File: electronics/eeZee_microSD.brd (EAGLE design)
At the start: 18.3 x 19.8 mm, 12 parts, among them U1 MCP1824S, U2 74HC4050, U4 MICROSD_CD

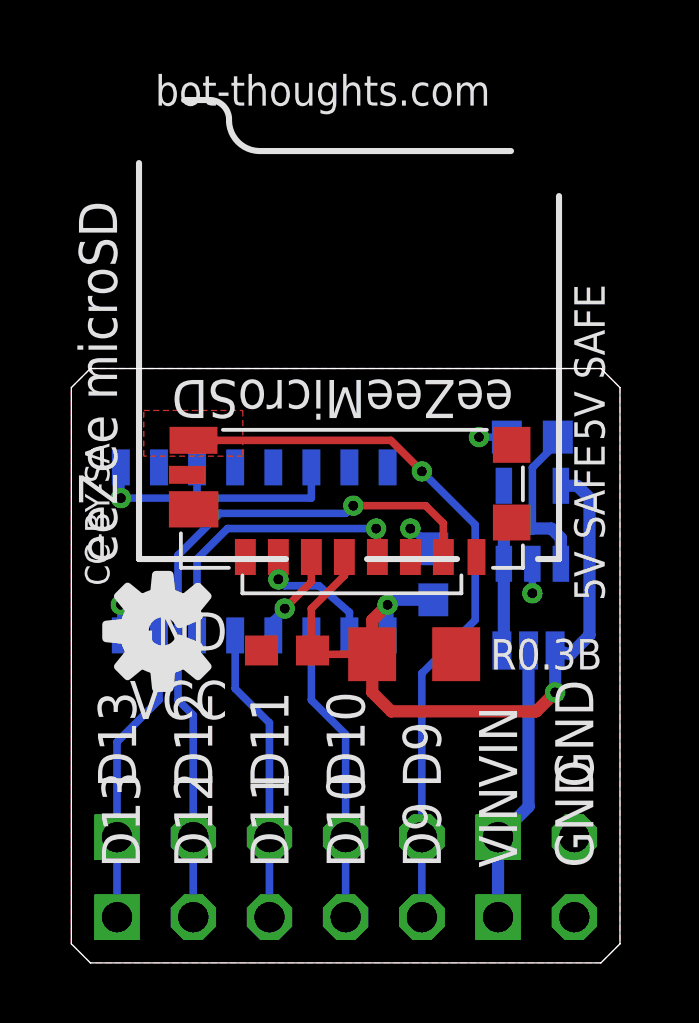
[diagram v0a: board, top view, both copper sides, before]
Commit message: Changed solder jumper due to overheat of MCP1824.
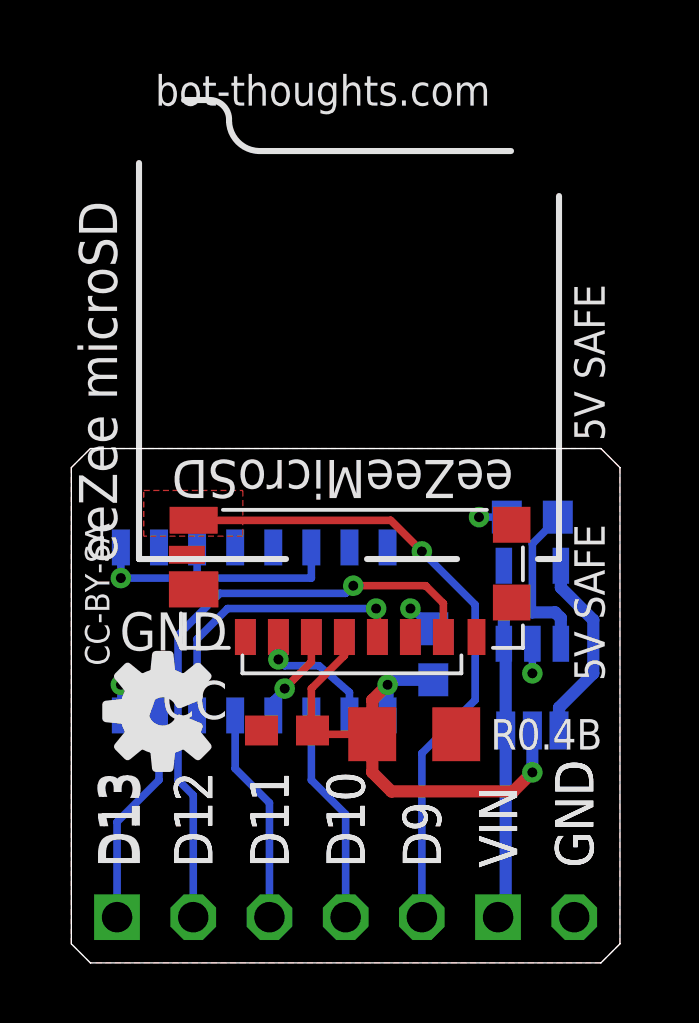
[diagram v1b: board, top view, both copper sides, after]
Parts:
- removed JP2: PWR, pinhead-2:1X02-S
- removed JP4: (no value), pinhead-2:1X05-S
- moved REG 2.67 mm to (15.4, 7.75)
- moved U4 2.67 mm to (9.65, 9.65)
- moved C1 2.67 mm to (11.4, 7.62)
- moved C2 2.67 mm to (12.1, 10.3)
- moved C3 2.67 mm to (7.19, 7.75)
- moved JP1 2.67 mm to (15.5, 1.52)
- moved R5 2.67 mm to (15.4, 14.9)
- moved U1 2.67 mm to (15.4, 11.9)
- moved U2 2.67 mm to (6.10, 11.0)
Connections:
- removed net VREGIN: R5.2, REG.3, U1.1, U1.3
- new net N$1: REG.1, U1.5
- net !CS_HV: no longer JP4.4
- net CD: no longer JP4.5
- net GND: no longer JP2.2
- net MISO: no longer JP4.2
- net MOSI_HV: no longer JP4.3
- net SCK_HV: no longer JP4.1
- net VCC: now also REG.2; no longer REG.1, U1.5
- net VIN: now also R5.2, REG.3, U1.1, U1.3; no longer JP2.1, REG.2
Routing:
- net VREGIN: track 10.2 -> 0.00 mm
- net VCC: track 26.5 -> 18.6 mm
- net VIN: track 9.31 -> 16.5 mm
- net N$1: track 0.00 -> 6.41 mm
- net MISO: track 23.2 -> 20.5 mm
- net CD: track 24.4 -> 21.7 mm
- net !CS_HV: track 9.87 -> 7.20 mm
- net SCK_HV: track 9.97 -> 7.30 mm
- net MOSI_HV: track 9.87 -> 7.20 mm
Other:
- board size 18.3 x 19.8 mm -> 18.3 x 17.1 mm
- board text added: "R0.4B"
- board text removed: "R0.3B"

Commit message: Fixed regulator overheat when BYP selected; removed jumper. Regulator outputs 3.3V when VIN=3.3V
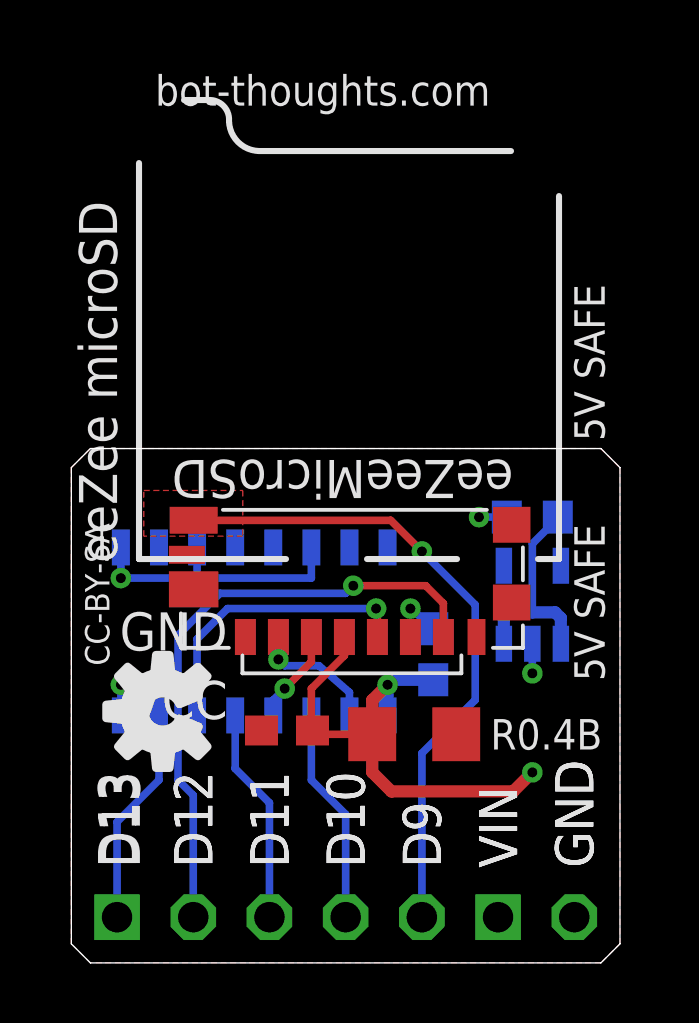
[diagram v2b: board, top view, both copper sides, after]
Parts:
- removed REG: BYP, SparkFun:SJ_3
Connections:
- removed net N$1: REG.1, U1.5
- net VCC: now also U1.5; no longer REG.2
- net VIN: no longer REG.3
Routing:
- net VIN: track 16.5 -> 7.74 mm
- net N$1: track 6.41 -> 0.00 mm
- net VCC: track 18.6 -> 17.2 mm
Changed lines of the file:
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@@
 </element>
 <element name="U4" library="bt_electromech" package="USD_SMALL" value="MICROSD_CD" x="9.652" y="9.652" smashed="yes" rot="R180"/>
-<element name="REG" library="SparkFun" package="SJ_3" value="BYP" x="15.367" y="7.747" smashed="yes" rot="MR0">
-<attribute name="NAME" x="17.145" y="6.731" size="0.8128" layer="26" font="vector" rot="MR90"/>
-<attribute name="VALUE" x="13.589" y="8.89" size="0.8128" layer="28" font="vector" rot="MR270"/>
-</element>
 </elements>
 <signals>
@@
 <wire x1="10.707" y1="9.437" x2="10.541" y2="9.271" width="0.4064" layer="16"/>
 <wire x1="10.541" y1="8.249" x2="10.541" y2="9.271" width="0.4064" layer="16"/>
-<contactref element="REG" pad="2"/>
-<wire x1="15.367" y1="7.747" x2="15.367" y2="6.35" width="0.4064" layer="16"/>
+<contactref element="U1" pad="5"/>
+<wire x1="12.065" y1="9.437" x2="16.317" y2="13.2381" width="0" layer="19" extent="16-16"/>
 </signal>
 <signal name="VIN">
@@
 <contactref element="U1" pad="3"/>
 <contactref element="U1" pad="1"/>
-<contactref element="REG" pad="3"/>
 <wire x1="16.317" y1="10.6379" x2="16.317" y2="11.496" width="0.4064" layer="16"/>
 <wire x1="16.317" y1="11.496" x2="16.129" y2="11.684" width="0.4064" layer="16"/>
@@
 <wire x1="16.217" y1="14.82" x2="15.367" y2="13.97" width="0.254" layer="16"/>
 <wire x1="15.367" y1="13.97" x2="15.367" y2="11.684" width="0.254" layer="16"/>
-<wire x1="14.478" y1="7.747" x2="14.478" y2="10.5769" width="0.4064" layer="16"/>
 <wire x1="14.478" y1="10.5769" x2="14.417" y2="10.6379" width="0.4064" layer="16"/>
-<wire x1="14.478" y1="7.747" x2="14.478" y2="1.778" width="0.4064" layer="16"/>
 <wire x1="14.478" y1="1.778" x2="14.224" y2="1.524" width="0.4064" layer="16"/>
+<wire x1="14.478" y1="1.778" x2="14.478" y2="10.5769" width="0" layer="19" extent="16-16"/>
 </signal>
 <signal name="CD">
@@
 <wire x1="11.684" y1="1.524" x2="11.684" y2="6.985" width="0.254" layer="16"/>
 </signal>
-<signal name="N$1">
-<contactref element="U1" pad="5"/>
-<contactref element="REG" pad="1"/>
-<wire x1="16.256" y1="7.747" x2="16.256" y2="8.509" width="0.4064" layer="16"/>
-<wire x1="16.256" y1="8.509" x2="17.399" y2="9.652" width="0.4064" layer="16"/>
-<wire x1="16.317" y1="13.2381" x2="16.317" y2="12.512" width="0.4064" layer="16"/>
-<wire x1="16.317" y1="12.512" x2="17.399" y2="11.43" width="0.4064" layer="16"/>
-<wire x1="17.399" y1="11.43" x2="17.399" y2="9.652" width="0.4064" layer="16"/>
-</signal>
 </signals>
